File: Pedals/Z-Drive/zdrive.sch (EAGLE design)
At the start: 30 parts, among them IC1 MC1458P, Q1 2N7000, Q2 2N7000

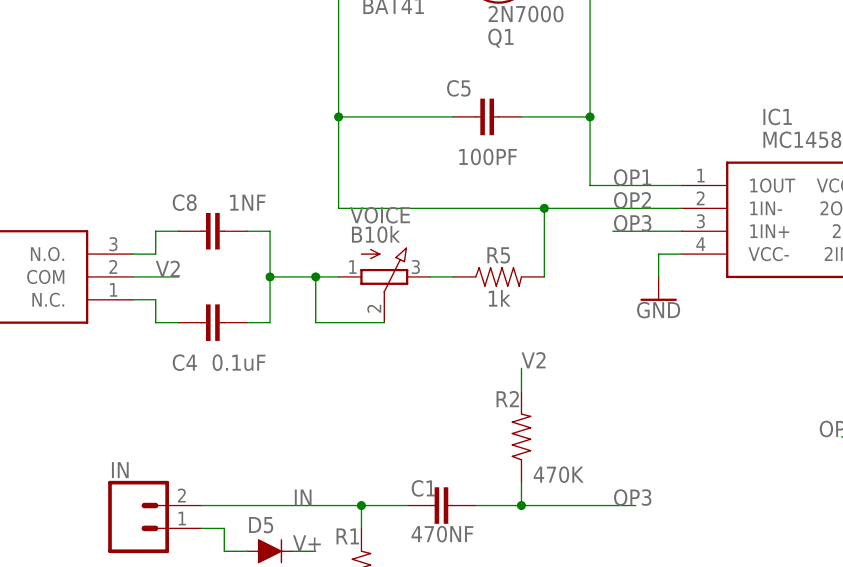
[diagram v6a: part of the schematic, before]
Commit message: Move resistor for greater impact of switch
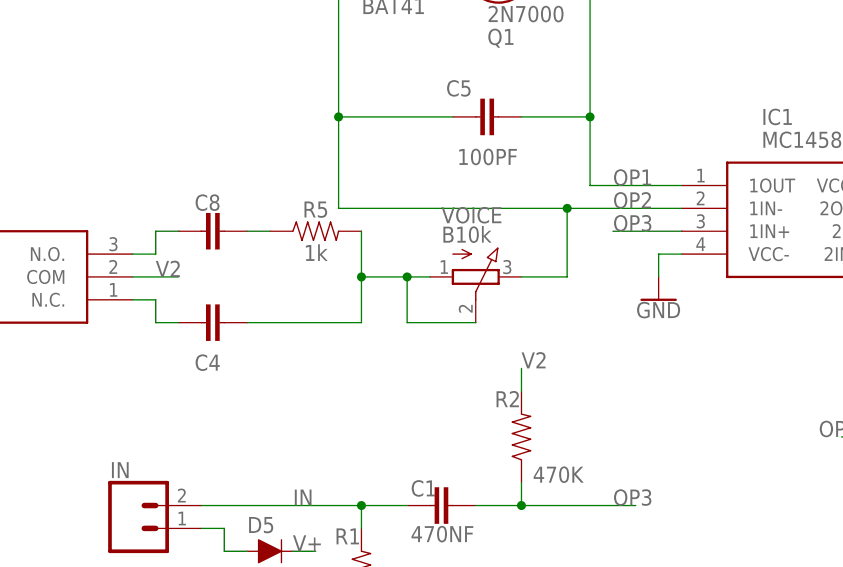
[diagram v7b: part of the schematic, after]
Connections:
- removed net N$7: C4.2, C8.2, VOICE.A, VOICE.S
- new net N$13: C4.2, R5.2, VOICE.A, VOICE.S
- net N$6: now also C8.2; no longer VOICE.E
- net OP2: now also VOICE.E; no longer R5.2
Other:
- moved on the sheet: R5, VOICE
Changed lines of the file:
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@@
 <attribute name="VALUE" x="96.52" y="75.946" size="1.778" layer="96" align="top-center"/>
 </instance>
-<instance part="R5" gate="G$1" x="0" y="73.66" smashed="yes">
-<attribute name="NAME" x="0" y="75.184" size="1.778" layer="95" font="vector" align="bottom-center"/>
-<attribute name="VALUE" x="0" y="72.136" size="1.778" layer="96" font="vector" align="top-center"/>
+<instance part="R5" gate="G$1" x="-20.32" y="78.74" smashed="yes">
+<attribute name="NAME" x="-20.32" y="80.264" size="1.778" layer="95" font="vector" align="bottom-center"/>
+<attribute name="VALUE" x="-20.32" y="77.216" size="1.778" layer="96" font="vector" align="top-center"/>
 </instance>
 <instance part="C4" gate="G$1" x="-30.48" y="68.58" smashed="yes" rot="R90">
-<attribute name="NAME" x="-33.401" y="65.024" size="1.778" layer="95" font="vector" rot="R180"/>
-<attribute name="VALUE" x="-25.781" y="65.024" size="1.778" layer="96" font="vector" rot="R180"/>
+<attribute name="NAME" x="-30.861" y="65.024" size="1.778" layer="95" font="vector" rot="R180"/>
 </instance>
 <instance part="C5" gate="G$1" x="0" y="91.44" smashed="yes" rot="R90">
@@
 <attribute name="VALUE" x="-11.43" y="148.59" size="1.778" layer="96"/>
 </instance>
-<instance part="VOICE" gate="G$1" x="-12.7" y="73.66" smashed="yes" rot="R270">
-<attribute name="NAME" x="-16.51" y="79.629" size="1.778" layer="95"/>
-<attribute name="VALUE" x="-16.51" y="77.47" size="1.778" layer="96"/>
+<instance part="VOICE" gate="G$1" x="-2.54" y="73.66" smashed="yes" rot="R270">
+<attribute name="NAME" x="-6.35" y="79.629" size="1.778" layer="95"/>
+<attribute name="VALUE" x="-6.35" y="77.47" size="1.778" layer="96"/>
 </instance>
 <instance part="TONE" gate="G$1" x="60.96" y="55.88" smashed="yes" rot="R90">
@@
 </instance>
 <instance part="C8" gate="G$1" x="-30.48" y="78.74" smashed="yes" rot="R90">
-<attribute name="NAME" x="-33.401" y="82.804" size="1.778" layer="95" font="vector" rot="R180"/>
-<attribute name="VALUE" x="-25.781" y="82.804" size="1.778" layer="96" font="vector" rot="R180"/>
+<attribute name="NAME" x="-30.861" y="82.804" size="1.778" layer="95" font="vector" rot="R180"/>
 </instance>
 <instance part="S1" gate="G$1" x="-40.64" y="71.12" smashed="yes" rot="R180">
@@
 </segment>
 </net>
-<net name="N$6" class="0">
-<segment>
-<pinref part="R5" gate="G$1" pin="1"/>
-<wire x1="-7.62" y1="73.66" x2="-5.08" y2="73.66" width="0.1524" layer="91"/>
-<pinref part="VOICE" gate="G$1" pin="E"/>
-</segment>
-</net>
-<net name="N$7" class="0">
-<segment>
-<wire x1="-17.78" y1="73.66" x2="-20.32" y2="73.66" width="0.1524" layer="91"/>
-<wire x1="-12.7" y1="68.58" x2="-20.32" y2="68.58" width="0.1524" layer="91"/>
-<wire x1="-20.32" y1="68.58" x2="-20.32" y2="73.66" width="0.1524" layer="91"/>
-<pinref part="VOICE" gate="G$1" pin="A"/>
-<pinref part="VOICE" gate="G$1" pin="S"/>
-<pinref part="C8" gate="G$1" pin="2"/>
-<wire x1="-27.94" y1="78.74" x2="-25.4" y2="78.74" width="0.1524" layer="91"/>
-<wire x1="-25.4" y1="78.74" x2="-25.4" y2="73.66" width="0.1524" layer="91"/>
-<wire x1="-25.4" y1="73.66" x2="-20.32" y2="73.66" width="0.1524" layer="91"/>
-<junction x="-20.32" y="73.66"/>
-<pinref part="C4" gate="G$1" pin="2"/>
-<wire x1="-27.94" y1="68.58" x2="-25.4" y2="68.58" width="0.1524" layer="91"/>
-<wire x1="-25.4" y1="68.58" x2="-25.4" y2="73.66" width="0.1524" layer="91"/>
-<junction x="-25.4" y="73.66"/>
-</segment>
-</net>
 <net name="N$8" class="0">
 <segment>
@@
 <junction x="-17.78" y="91.44"/>
 <pinref part="IC1" gate="G$1" pin="1IN-"/>
-<wire x1="20.32" y1="81.28" x2="5.08" y2="81.28" width="0.1524" layer="91"/>
-<wire x1="5.08" y1="81.28" x2="5.08" y2="73.66" width="0.1524" layer="91"/>
-<pinref part="R5" gate="G$1" pin="2"/>
-<wire x1="-17.78" y1="81.28" x2="5.08" y2="81.28" width="0.1524" layer="91"/>
-<junction x="5.08" y="81.28"/>
+<wire x1="-17.78" y1="81.28" x2="7.62" y2="81.28" width="0.1524" layer="91"/>
 <label x="12.7" y="81.28" size="1.778" layer="95"/>
 <pinref part="GAIN" gate="G$1" pin="A"/>
+<pinref part="VOICE" gate="G$1" pin="E"/>
+<wire x1="7.62" y1="81.28" x2="20.32" y2="81.28" width="0.1524" layer="91"/>
+<wire x1="2.54" y1="73.66" x2="7.62" y2="73.66" width="0.1524" layer="91"/>
+<wire x1="7.62" y1="73.66" x2="7.62" y2="81.28" width="0.1524" layer="91"/>
+<junction x="7.62" y="81.28"/>
 </segment>
 </net>
@@
 </segment>
 </net>
+<net name="N$13" class="0">
+<segment>
+<pinref part="C4" gate="G$1" pin="2"/>
+<wire x1="-7.62" y1="73.66" x2="-10.16" y2="73.66" width="0.1524" layer="91"/>
+<wire x1="-2.54" y1="68.58" x2="-10.16" y2="68.58" width="0.1524" layer="91"/>
+<wire x1="-10.16" y1="68.58" x2="-10.16" y2="73.66" width="0.1524" layer="91"/>
+<pinref part="VOICE" gate="G$1" pin="A"/>
+<pinref part="VOICE" gate="G$1" pin="S"/>
+<junction x="-10.16" y="73.66"/>
+<wire x1="-15.24" y1="73.66" x2="-10.16" y2="73.66" width="0.1524" layer="91"/>
+<wire x1="-15.24" y1="78.74" x2="-15.24" y2="73.66" width="0.1524" layer="91"/>
+<junction x="-15.24" y="73.66"/>
+<wire x1="-27.94" y1="68.58" x2="-15.24" y2="68.58" width="0.1524" layer="91"/>
+<wire x1="-15.24" y1="68.58" x2="-15.24" y2="73.66" width="0.1524" layer="91"/>
+<pinref part="R5" gate="G$1" pin="2"/>
+</segment>
+</net>
+<net name="N$6" class="0">
+<segment>
+<pinref part="C8" gate="G$1" pin="2"/>
+<pinref part="R5" gate="G$1" pin="1"/>
+<wire x1="-27.94" y1="78.74" x2="-25.4" y2="78.74" width="0.1524" layer="91"/>
+</segment>
+</net>

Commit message: Updated to larger cap footprints for Headmaster
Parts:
- C4: value 0.1uF -> 0.1UF; device SparkFun-Capacitors:0.1UF-KIT-EZ-50V-20% -> Custom-Parts:0.1UF
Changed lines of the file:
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@@
 <part name="GND4" library="SparkFun-PowerSymbols" library_urn="urn:adsk.eagle:library:530" deviceset="GND" device=""/>
 <part name="R5" library="SparkFun-Resistors" library_urn="urn:adsk.eagle:library:532" deviceset="1KOHM" device="-HORIZ-1/4W-5%" package3d_urn="urn:adsk.eagle:package:39658/1" value="1k"/>
-<part name="C4" library="SparkFun-Capacitors" library_urn="urn:adsk.eagle:library:510" deviceset="0.1UF" device="-KIT-EZ-50V-20%" package3d_urn="urn:adsk.eagle:package:37428/1" value="0.1uF"/>
+<part name="C4" library="Custom-Parts" deviceset="0.1UF" device="" value="0.1UF"/>
 <part name="C5" library="Custom-Parts" deviceset="100PF" device=""/>
 <part name="GND5" library="SparkFun-PowerSymbols" library_urn="urn:adsk.eagle:library:530" deviceset="GND" device=""/>
